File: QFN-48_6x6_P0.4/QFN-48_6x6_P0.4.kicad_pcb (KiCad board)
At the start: 2 copper layers, 25.4 x 66 mm, 6 parts, among them J101 Conn_01x26, J102 Conn_01x26, J103 Conn_01x26, J104 Conn_01x26, U101 QFN-48

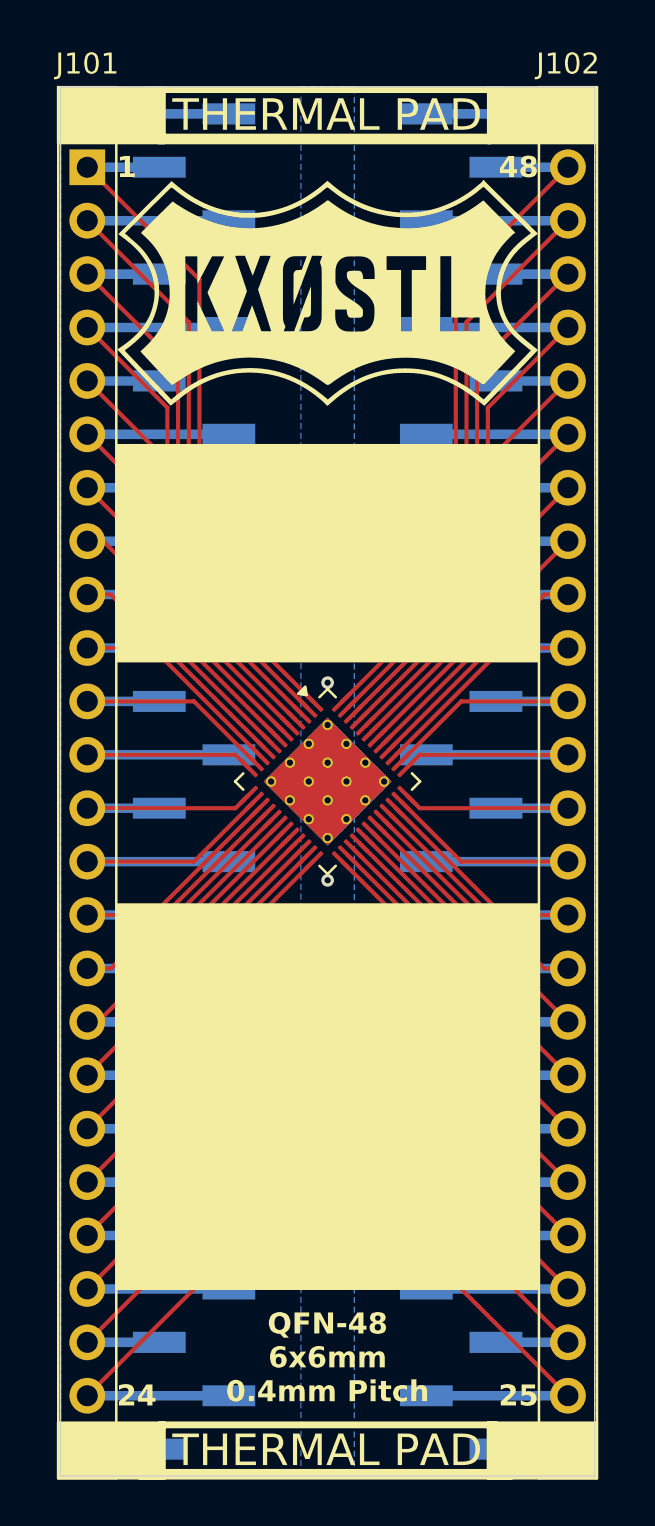
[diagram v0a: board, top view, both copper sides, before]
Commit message: Created SMDIP-16, QFP-48, QFP-32, QFN-80, QFN-68, QFN-64, QFN-60, QFN-56, QFN-48, QFN-36, QFN-28, QFN-20, QFP-32, QFP-48
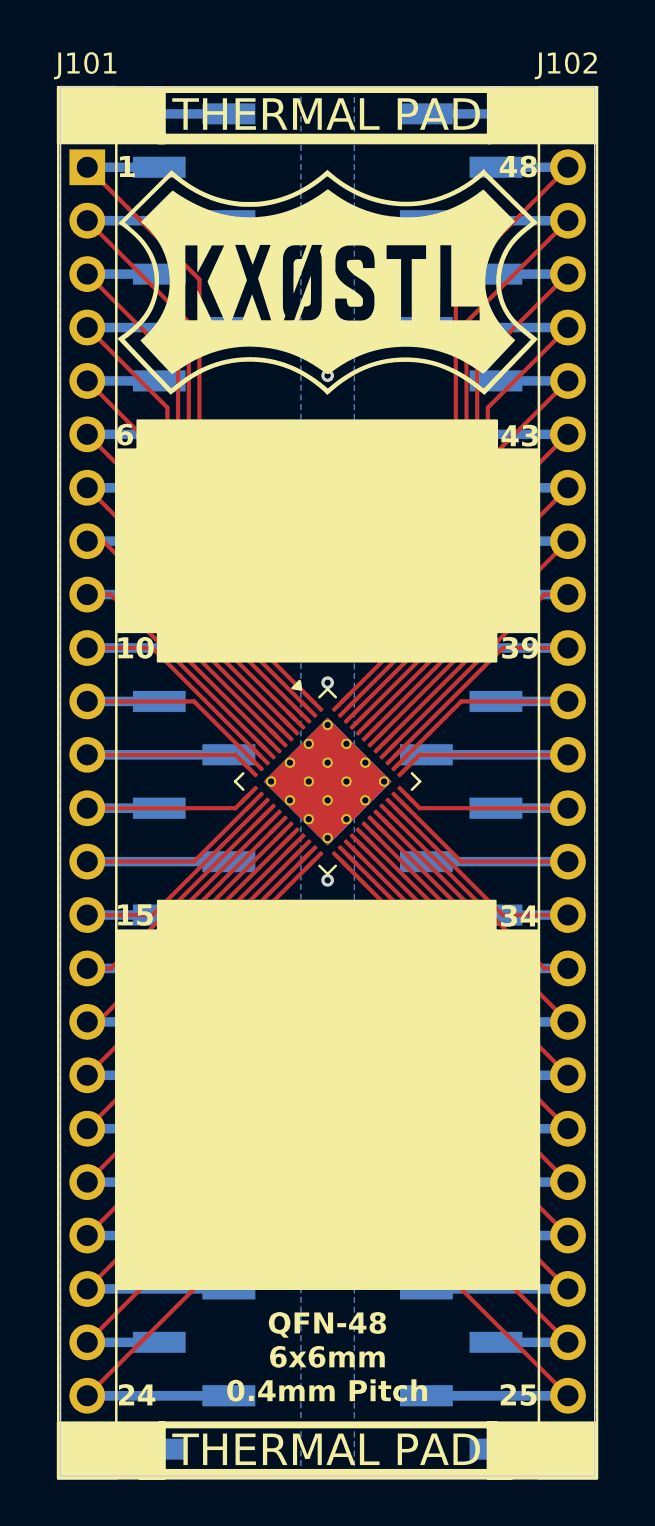
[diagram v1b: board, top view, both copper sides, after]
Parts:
- moved G*** 0.52 mm to (138.4, 96.9)
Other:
- board text added: "10"
- board text added: "15"
- board text added: "34"
- board text added: "39"
- board text added: "43"
- board text added: "6"
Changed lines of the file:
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@@
 		(fp_poly
 			(pts
-				(xy -3.61 -2.199999) (xy -3.94 -1.96) (xy -3.94 -2.44)
+				(xy -3.99 -2.199999) (xy -4.32 -1.96) (xy -4.32 -2.44)
 			)
 			(stroke
@@
 	(footprint "libraries:LogoSmall"
 		(layer "F.Cu")
-		(at 138.430934 97.417496)
+		(at 138.430934 96.897121)
 		(property "Reference" "G***"
 			(at 0 0 0)
@@
 	)
 	(gr_rect
-		(start 128.397 126.492)
+		(start 130.357355 106.256355)
+		(end 146.453355 114.943355)
+		(stroke
+			(width 0.1)
+			(type solid)
+		)
+		(fill yes)
+		(layer "F.SilkS")
+	)
+	(gr_rect
+		(start 128.397 127.732)
 		(end 148.463 144.78)
 		(stroke
@@
 	)
 	(gr_rect
-		(start 128.397 104.648)
-		(end 148.463 114.935)
+		(start 129.387 103.48)
+		(end 146.483 112.167)
+		(stroke
+			(width 0.1)
+			(type solid)
+		)
+		(fill yes)
+		(layer "F.SilkS")
+	)
+	(gr_rect
+		(start 130.362 126.323)
+		(end 146.418 135.01)
+		(stroke
+			(width 0.1)
+			(type solid)
+		)
+		(fill yes)
+		(layer "F.SilkS")
+	)
+	(gr_rect
+		(start 128.397 104.858)
+		(end 148.463 113.545)
 		(stroke
 			(width 0.1)
@@
 		(layer "Edge.Cuts")
 	)
+	(gr_text "34"
+		(at 148.5 127.08 0)
+		(layer "F.SilkS" knockout)
+		(effects
+			(font
+				(size 1 1)
+				(thickness 0.2)
+				(bold yes)
+			)
+			(justify right)
+		)
+	)
 	(gr_text "48"
 		(at 148.463 91.44 0)
@@
 		)
 	)
+	(gr_text "10"
+		(at 128.32 114.33 0)
+		(layer "F.SilkS" knockout)
+		(effects
+			(font
+				(size 1 1)
+				(thickness 0.2)
+				(bold yes)
+			)
+			(justify left)
+		)
+	)
 	(gr_text "QFN-48\n6x6mm\n0.4mm Pitch"
 		(at 138.43 150.241 0)
@@
 		)
 	)
+	(gr_text "43"
+		(at 148.54 104.24 0)
+		(layer "F.SilkS" knockout)
+		(effects
+			(font
+				(size 1 1)
+				(thickness 0.2)
+				(bold yes)
+			)
+			(justify right)
+		)
+	)
+	(gr_text "15"
+		(at 128.31 127.03 0)
+		(layer "F.SilkS" knockout)
+		(effects
+			(font
+				(size 1 1)
+				(thickness 0.2)
+				(bold yes)
+			)
+			(justify left)
+		)
+	)
 	(gr_text "THERMAL PAD"
 		(at 138.4215 152.463375 0)
@@
 		)
 	)
+	(gr_text "6"
+		(at 128.3 104.19 0)
+		(layer "F.SilkS" knockout)
+		(effects
+			(font
+				(size 1 1)
+				(thickness 0.2)
+				(bold yes)
+			)
+			(justify left)
+		)
+	)
+	(gr_text "39"
+		(at 148.55 114.33 0)
+		(layer "F.SilkS" knockout)
+		(effects
+			(font
+				(size 1 1)
+				(thickness 0.2)
+				(bold yes)
+			)
+			(justify right)
+		)
+	)
